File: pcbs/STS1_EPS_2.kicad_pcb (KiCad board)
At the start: 4 copper layers, 81 x 85 mm, 77 parts, among them J1 Inter-EPS, J2 DS1, J3 DS2, J4 DS3, J5 DS4, J6 RBF, J7 Antenna Deployment, J8 UCI, Q1 2N7002, Q10 2N7002, Q11 SI7272DP-T1-GE3, Q12 SI7272DP-T1-GE3, Q13 2N7002, Q14 2N7002, Q15 2N7002, Q16 BSS83P, Q17 2N7002, Q18 2N7002, Q19 SI7272DP-T1-GE3, Q2 SI7135DP-T1-GE3, Q20 2N7002, Q21 2N7002, Q3 SI7135DP-T1-GE3, Q4 SI7135DP-T1-GE3, Q5 SI7135DP-T1-GE3, Q6 2N7002, Q7 2N7002, Q8 BSS83P, Q9 2N7002, U1 LTC6995IDCB-1, U2 4072, U27 TPS2420RSAT, U3 MIC841

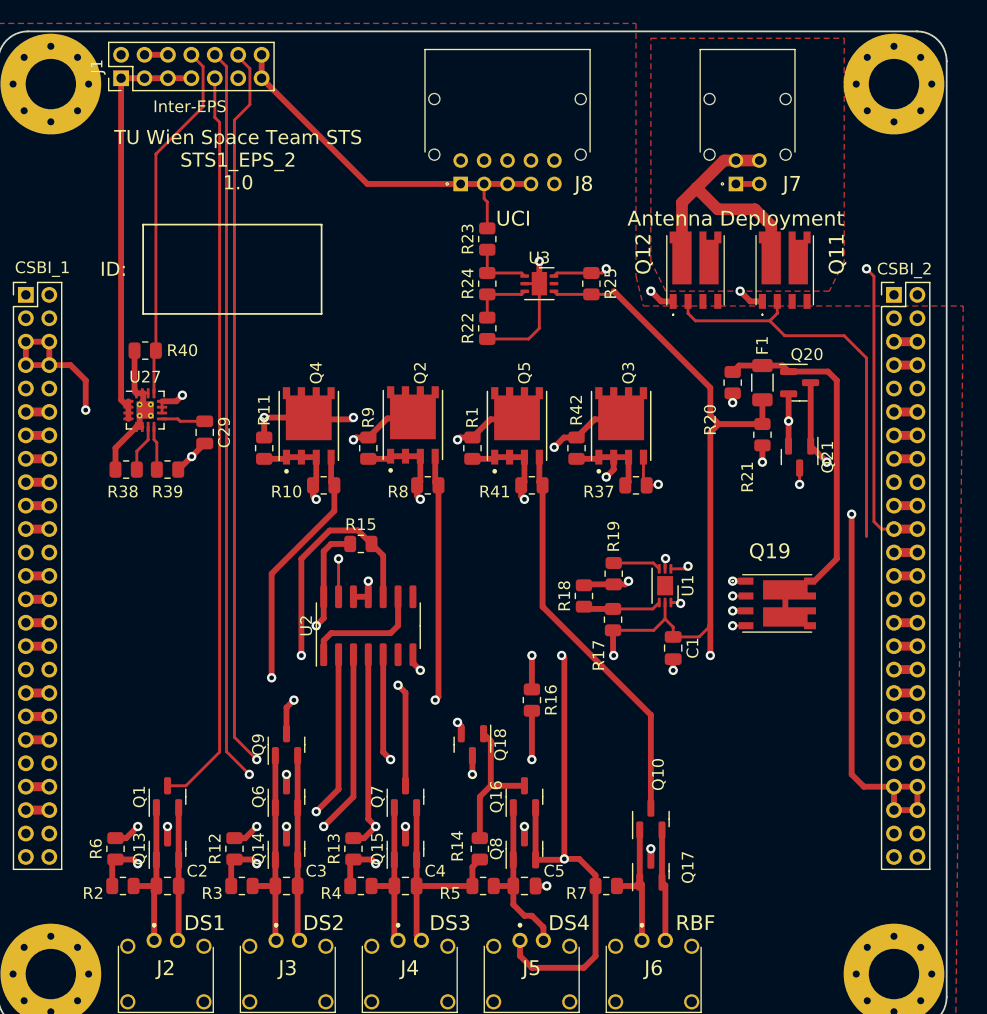
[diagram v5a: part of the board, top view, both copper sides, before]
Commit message: Cleared all DRC errors of STS1_EPS_1.
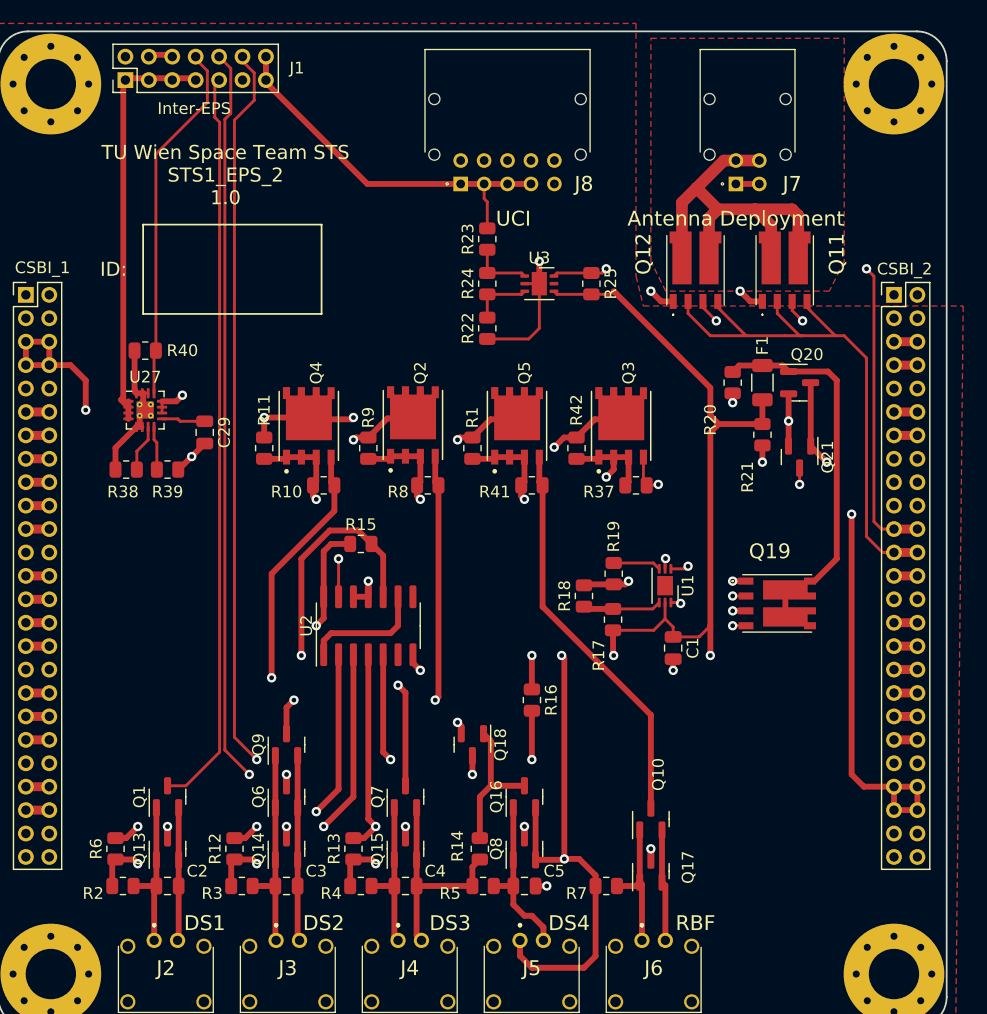
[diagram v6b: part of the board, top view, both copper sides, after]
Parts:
- moved J1 0.40 mm to (127.0, 46.0)
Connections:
- CSBI_2 pad 24: unconnected-(CSBI_2-Pad24) -> /EPS_ANT_DEPLOY
- Q11 pad 10: (no net) -> /Antenna Deployment/ANT_DEPLOY-
- Q11 pad 12: (no net) -> /Antenna Deployment/ANT_DEPLOY-
- Q11 pad 3: (no net) -> GND
- Q11 pad 4: (no net) -> /EPS_ANT_DEPLOY
- Q11 pad 5: (no net) -> /Antenna Deployment/ANT_DEPLOY-
- Q11 pad 6: (no net) -> /Antenna Deployment/ANT_DEPLOY-
- Q12 pad 10: (no net) -> /Antenna Deployment/ANT_DEPLOY-
- Q12 pad 12: (no net) -> /Antenna Deployment/ANT_DEPLOY-
- Q12 pad 3: (no net) -> GND
- Q12 pad 4: (no net) -> /EPS_ANT_DEPLOY
- Q12 pad 5: (no net) -> /Antenna Deployment/ANT_DEPLOY-
- Q12 pad 6: (no net) -> /Antenna Deployment/ANT_DEPLOY-
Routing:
- net /EPS_ANT_DEPLOY: track 35.0 -> 49.8 mm
- net /Antenna Deployment/ANT_DEPLOY-: track 24.0 -> 36.7 mm
- net GND: track 108.3 -> 112.5 mm, vias 15 -> 17
- net unconnected-(CSBI_2-Pad24): track 2.00 -> 0.00 mm
- net unconnected-(CSBI_2-Pad19): track 2.00 -> 0.00 mm
- net unconnected-(CSBI_2-Pad15): track 2.00 -> 0.00 mm

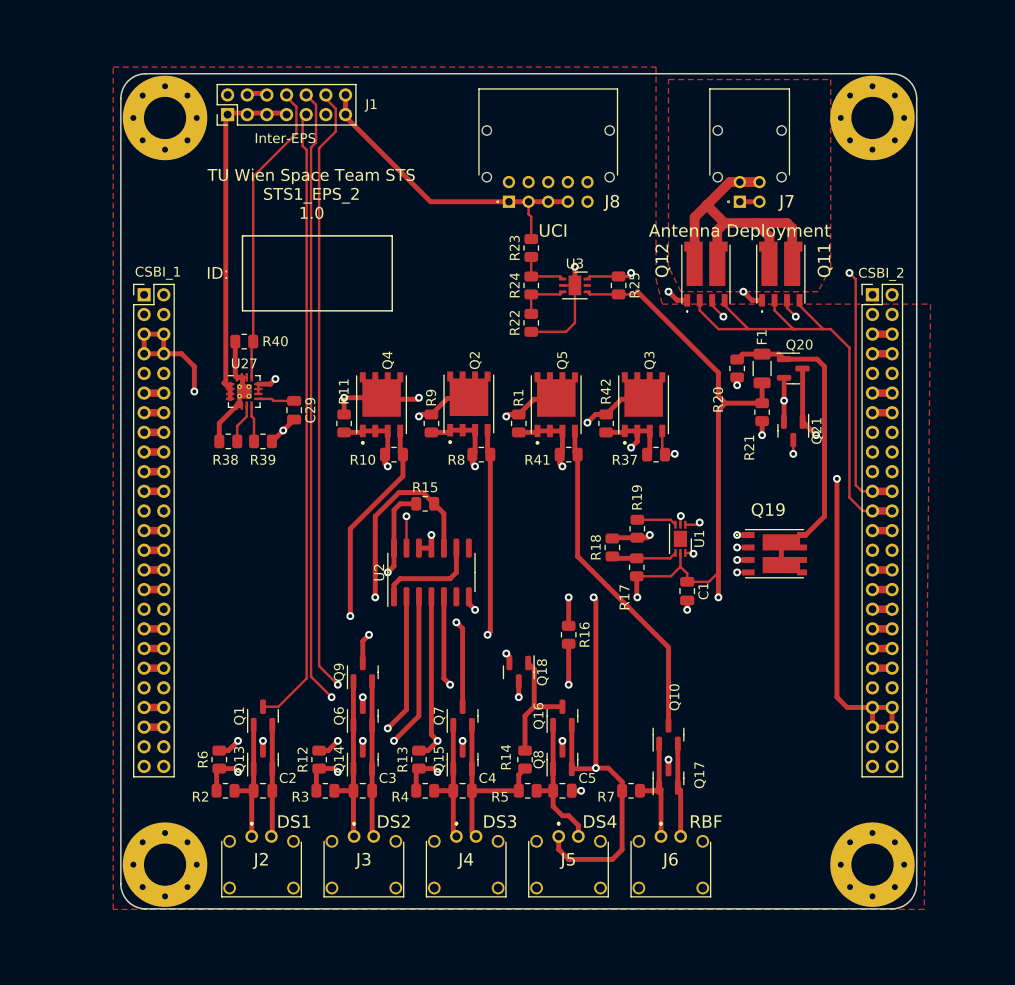
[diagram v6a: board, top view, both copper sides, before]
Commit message: Reworked STS1_EPS_2. - Added Capacitor bank - Thickened some load bearing copper traces.
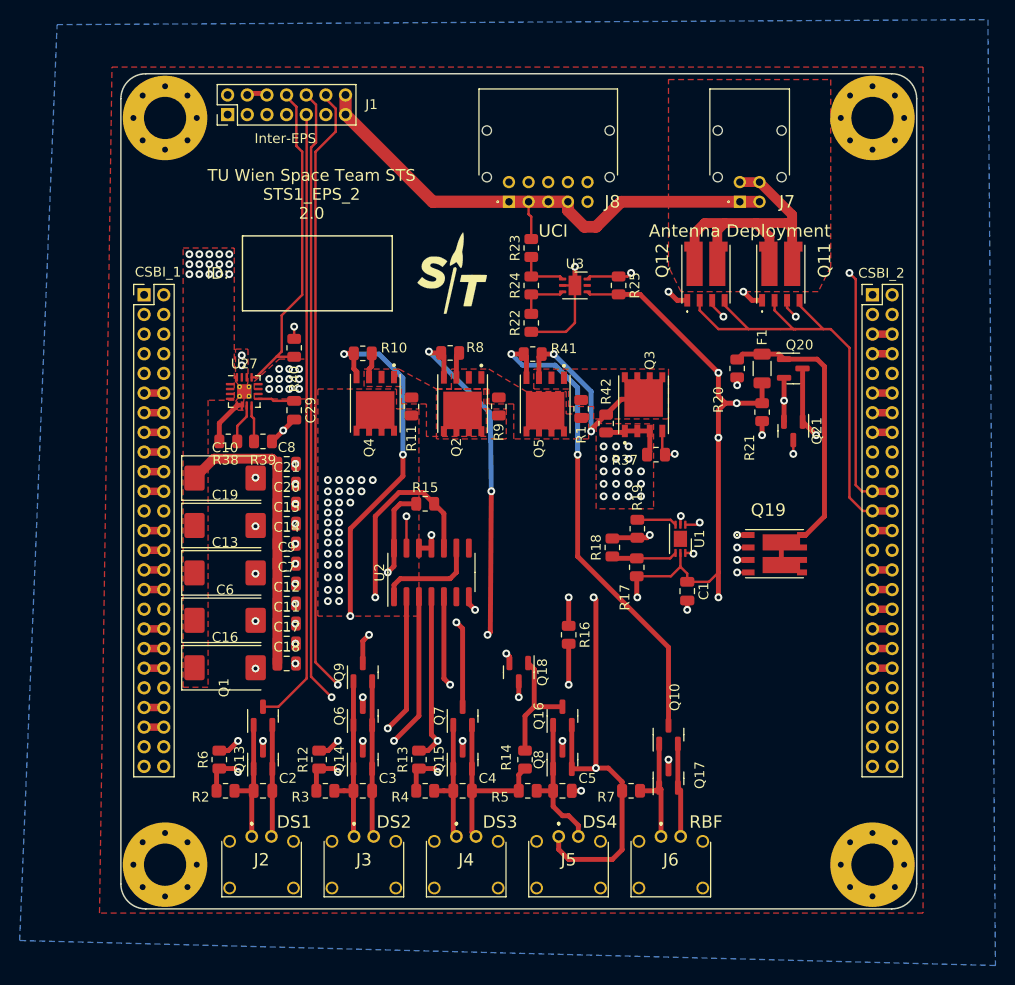
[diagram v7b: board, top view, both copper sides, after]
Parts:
- added C10: C_Polarized, Capacitor_Tantalum_SMD:CP_EIA-7343-43_Kemet-X, F.Cu at (126.7, 83.0)
- added C11: C, Capacitor_SMD:C_0805_2012Metric, F.Cu at (133.0, 97.8)
- added C12: C, Capacitor_SMD:C_0805_2012Metric, F.Cu at (133.0, 95.7)
- added C13: C_Polarized, Capacitor_Tantalum_SMD:CP_EIA-7343-43_Kemet-X, F.Cu at (126.7, 92.6)
- added C14: C, Capacitor_SMD:C_0805_2012Metric, F.Cu at (133.0, 89.6)
- added C15: C, Capacitor_SMD:C_0805_2012Metric, F.Cu at (133.0, 87.6)
- added C16: C_Polarized, Capacitor_Tantalum_SMD:CP_EIA-7343-43_Kemet-X, F.Cu at (126.7, 102.3)
- added C17: C, Capacitor_SMD:C_0805_2012Metric, F.Cu at (133.0, 99.8)
- added C18: C, Capacitor_SMD:C_0805_2012Metric, F.Cu at (133.0, 101.8)
- added C19: C_Polarized, Capacitor_Tantalum_SMD:CP_EIA-7343-43_Kemet-X, F.Cu at (126.7, 87.8)
- added C20: C, Capacitor_SMD:C_0805_2012Metric, F.Cu at (133.0, 85.6)
- added C21: C, Capacitor_SMD:C_0805_2012Metric, F.Cu at (133.0, 83.5)
- added C6: C_Polarized, Capacitor_Tantalum_SMD:CP_EIA-7343-43_Kemet-X, F.Cu at (126.7, 97.4)
- added C7: C, Capacitor_SMD:C_0805_2012Metric, F.Cu at (133.0, 93.7)
- added C8: C, Capacitor_SMD:C_0805_2012Metric, F.Cu at (133.0, 81.5)
- added C9: C, Capacitor_SMD:C_0805_2012Metric, F.Cu at (133.0, 91.7)
- added G***: LOGO, STS_Logo:STLogo_7x8, F.Cu at (149.9, 62.1)
- moved R41 10.9 mm to (158.1, 70.3), turned to 180 degrees
- moved R8 10.8 mm to (149.6, 70.2), turned to 180 degrees
- moved R10 10.8 mm to (140.8, 70.3), turned to 180 degrees
- moved R11 7.07 mm to (145.7, 75.7), turned to -90 degrees
- moved R9 7.07 mm to (154.6, 75.7), turned to -90 degrees
- moved R1 6.52 mm to (163.0, 75.9), turned to -90 degrees
- moved R40 5.12 mm to (133.8, 69.7), turned to 90 degrees
- moved Q5 1.12 mm to (159.3, 75.4), turned to -90 degrees
- moved Q4 0.65 mm to (142.0, 75.3), turned to -90 degrees
- moved Q2 0.64 mm to (150.9, 75.4), turned to -90 degrees
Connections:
- J7 pad 1: /BAT_RAW -> /BATT_RAW
- J7 pad 2: /BAT_RAW -> /BATT_RAW
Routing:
- net /Bus Gate/VOUT_GATED: track 123.4 -> 0.22 mm, vias 4 -> 30
- net Net-(Q3-Pad1): track 54.0 -> 7.03 mm, vias 2 -> 29
- net /BATT_RAW: track 32.6 -> 54.3 mm
- net Net-(Q2-Pad1): track 20.6 -> 2.60 mm, vias 2 -> 0
- net Net-(Q2-Pad5): track 20.6 -> 2.73 mm, vias 2 -> 0
- net /RBF_SIGNAL_1: track 33.9 -> 50.2 mm, vias 0 -> 2
- net /DS3_SIGNAL_1: track 41.1 -> 56.9 mm, vias 2 -> 4
- net /DS2_SIGNAL_2: track 36.3 -> 50.2 mm, vias 2 -> 4
- net /INTERNAL_V: track 35.8 -> 29.8 mm, vias 0 -> 15
- net GND: track 112.5 -> 108.3 mm, vias 17 -> 36
- net /VOUT_I: track 31.4 -> 33.9 mm
- net unconnected-(CSBI_2-Pad15): track 0.00 -> 2.00 mm
- net /BAT_RAW: track 2.00 -> 0.00 mm
- net /Antenna Deployment/ANT_DEPLOY-: track 36.7 -> 36.0 mm
- net Net-(Q3-Pad5): track 20.5 -> 20.0 mm
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- added copper zone on B.Cu, net (none)
- added copper zone on F.Cu, net (none)
- added copper zone on F.Cu, net /Bus Gate/VOUT_GATED
- added copper zone on F.Cu, net /INTERNAL_V
- added copper zone on In2.Cu, net /INTERNAL_V
- added copper zone on F.Cu, net GND
- added copper zone on F.Cu, net Net-(Q2-Pad1)
- added copper zone on F.Cu, net Net-(Q2-Pad5)
- added copper zone on F.Cu, net Net-(Q3-Pad1)
- added copper zone on In2.Cu, net Net-(Q3-Pad1)
- added copper zone on F.Cu, net Net-(Q3-Pad5)
- removed copper zone on F.Cu, net /+5V
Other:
- board text added: "TU Wien Space Team STS STS1_EPS_2 2.0"
- board text removed: "TU Wien Space Team STS STS1_EPS_2 1.0"

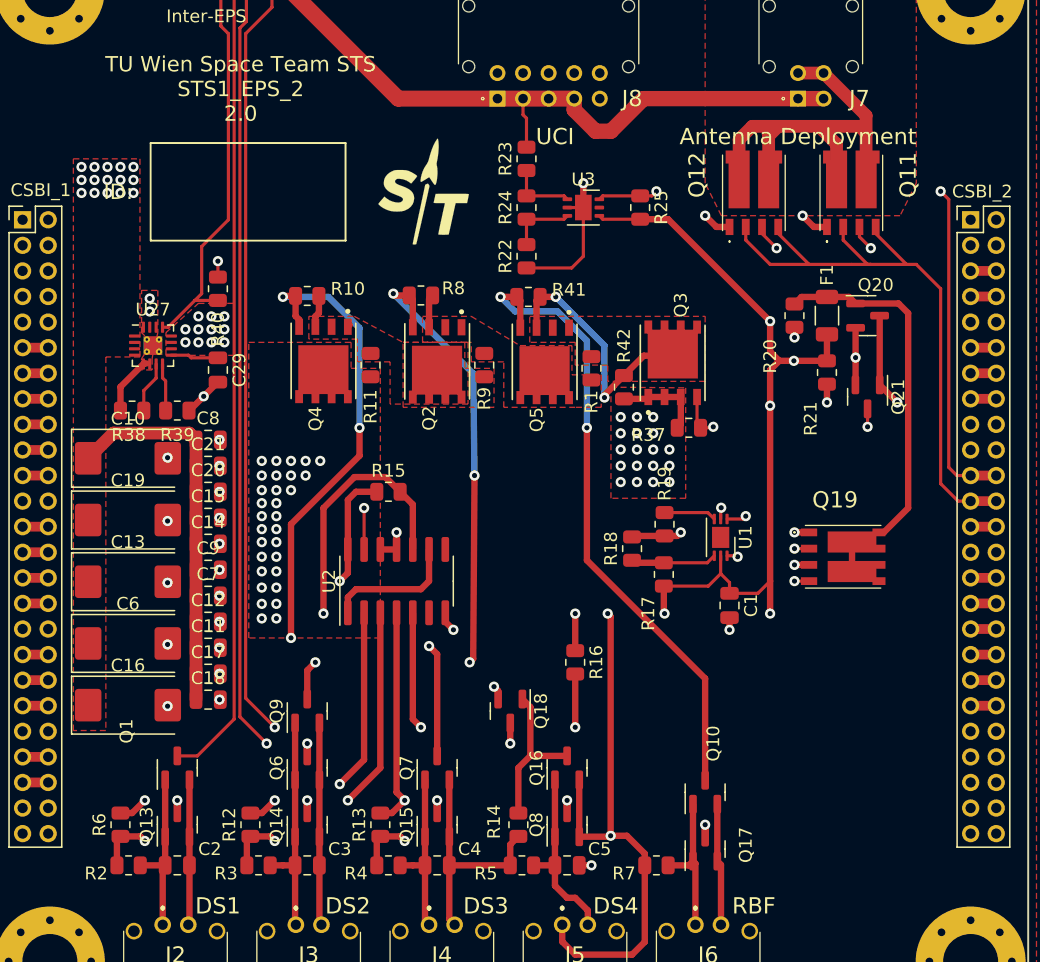
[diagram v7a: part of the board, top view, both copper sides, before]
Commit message: Added test points to STS1_EPS_2.
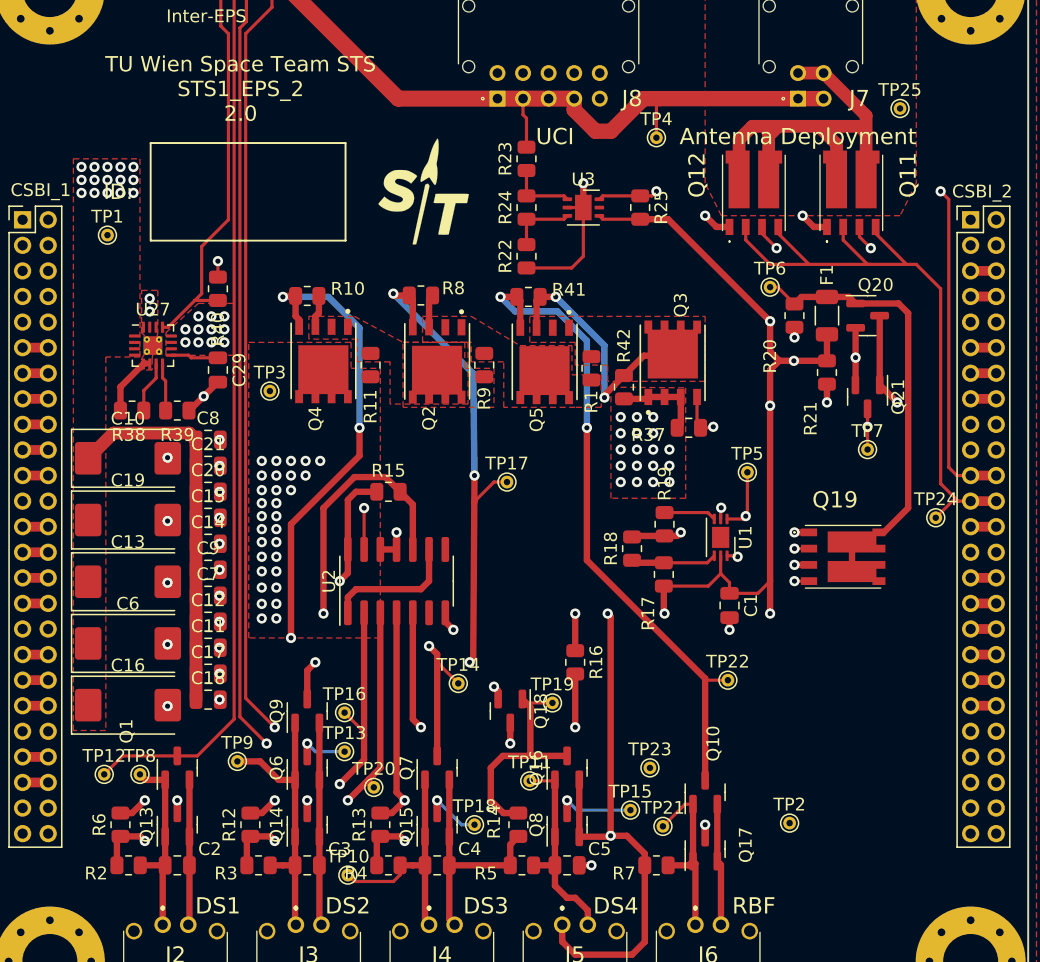
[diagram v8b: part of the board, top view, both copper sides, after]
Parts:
- added TP1: TestPoint, TestPoint:TestPoint_THTPad_D1.0mm_Drill0.5mm, F.Cu at (125.1, 65.5)
- added TP10: TestPoint, TestPoint:TestPoint_THTPad_D1.0mm_Drill0.5mm, F.Cu at (143.9, 115.5)
- added TP11: TestPoint, TestPoint:TestPoint_THTPad_D1.0mm_Drill0.5mm, F.Cu at (158.2, 108.2)
- added TP12: TestPoint, TestPoint:TestPoint_THTPad_D1.0mm_Drill0.5mm, F.Cu at (124.9, 107.7)
- added TP13: TestPoint, TestPoint:TestPoint_THTPad_D1.0mm_Drill0.5mm, F.Cu at (143.7, 105.9)
- added TP14: TestPoint, TestPoint:TestPoint_THTPad_D1.0mm_Drill0.5mm, F.Cu at (152.6, 100.6)
- added TP15: TestPoint, TestPoint:TestPoint_THTPad_D1.0mm_Drill0.5mm, F.Cu at (166.0, 110.5)
- added TP16: TestPoint, TestPoint:TestPoint_THTPad_D1.0mm_Drill0.5mm, F.Cu at (143.7, 102.8)
- added TP17: TestPoint, TestPoint:TestPoint_THTPad_D1.0mm_Drill0.5mm, F.Cu at (156.4, 84.8)
- added TP18: TestPoint, TestPoint:TestPoint_THTPad_D1.0mm_Drill0.5mm, F.Cu at (153.8, 111.6)
- added TP19: TestPoint, TestPoint:TestPoint_THTPad_D1.0mm_Drill0.5mm, F.Cu at (159.9, 102.1)
- added TP2: TestPoint, TestPoint:TestPoint_THTPad_D1.0mm_Drill0.5mm, F.Cu at (178.5, 111.5)
- added TP20: TestPoint, TestPoint:TestPoint_THTPad_D1.0mm_Drill0.5mm, F.Cu at (146.0, 108.7)
- added TP21: TestPoint, TestPoint:TestPoint_THTPad_D1.0mm_Drill0.5mm, F.Cu at (168.6, 111.7)
- added TP22: TestPoint, TestPoint:TestPoint_THTPad_D1.0mm_Drill0.5mm, F.Cu at (173.7, 100.3)
- added TP23: TestPoint, TestPoint:TestPoint_THTPad_D1.0mm_Drill0.5mm, F.Cu at (167.6, 107.2)
- added TP24: TestPoint, TestPoint:TestPoint_THTPad_D1.0mm_Drill0.5mm, F.Cu at (189.9, 87.6)
- added TP25: TestPoint, TestPoint:TestPoint_THTPad_D1.0mm_Drill0.5mm, F.Cu at (187.1, 55.6)
- added TP3: TestPoint, TestPoint:TestPoint_THTPad_D1.0mm_Drill0.5mm, F.Cu at (137.8, 77.7)
- added TP4: TestPoint, TestPoint:TestPoint_THTPad_D1.0mm_Drill0.5mm, F.Cu at (168.1, 57.9)
- added TP5: TestPoint, TestPoint:TestPoint_THTPad_D1.0mm_Drill0.5mm, F.Cu at (175.2, 84.0)
- added TP6: TestPoint, TestPoint:TestPoint_THTPad_D1.0mm_Drill0.5mm, F.Cu at (177.0, 69.6)
- added TP7: TestPoint, TestPoint:TestPoint_THTPad_D1.0mm_Drill0.5mm, F.Cu at (184.6, 82.3)
- added TP8: TestPoint, TestPoint:TestPoint_THTPad_D1.0mm_Drill0.5mm, F.Cu at (127.7, 107.7)
- added TP9: TestPoint, TestPoint:TestPoint_THTPad_D1.0mm_Drill0.5mm, F.Cu at (135.3, 106.7)
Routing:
- net /DS1_SIGNAL_1: track 63.0 -> 69.4 mm
- net /DS4_SIGNAL_2: track 12.4 -> 18.6 mm
- net /DS4_SIGNAL_1: track 88.6 -> 93.8 mm
- net /Deployment Switches + RBF/DS3+: track 13.4 -> 18.7 mm
- net /Deployment Switches + RBF/DS2+: track 17.7 -> 22.9 mm
- net /DS3_SIGNAL_2: track 20.8 -> 24.5 mm
- net Net-(U1-Pad1): track 36.7 -> 40.2 mm
- net /DS2_SIGNAL_2: track 50.2 -> 53.4 mm
- net /DS2_SIGNAL_1: track 66.9 -> 70.1 mm
- net /BATT_RAW: track 54.3 -> 57.5 mm
- net /Deployment Switches + RBF/RBF+: track 11.6 -> 14.7 mm
- net /DS3_SIGNAL_1: track 56.9 -> 59.9 mm
- net Net-(F1-Pad2): track 30.1 -> 32.6 mm
- net /DS1_SIGNAL_2: track 33.2 -> 35.6 mm
- net /EPS_ANT_DEPLOY: track 49.8 -> 52.1 mm
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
